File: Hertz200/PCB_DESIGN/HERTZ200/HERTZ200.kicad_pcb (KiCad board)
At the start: 2 copper layers, 7.1 x 7.3 mm, 99 parts, among them IC1 BD33HC5MEFJ-ME2, J1 SMA_CONNECTOR, J2 SIM_Card, J3 SMA_CONNECTOR, J4 DCJ250-10-A-K1-K, J5 USB_B_Micro, J6 GPIO_PINS, J7 SWD_PINS, Q1 Si2312DS, Q2 BC847, Q3 Si2312DS, Q4 CSD25302Q2, SW1 SW_Push, SW2 SW_Push, U1 STM32L431CCUx, U2 SIM7020E, U3 TXB0104PW, U4 SIM68M, U5 BQ24195LRGER, U6 HTS221

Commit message: layout02
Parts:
- C10, C14, C15, C2, C21, C22, C23, C24, C25, C26, C3, C4, C5, C6, C7, C8, C9, D4, D6, R25: moved to B.Cu
- SW2: footprint TS04-66-75-BK-160-SMT:SW_TS04-66-75-BK-160-SMT -> TL3305AF160QG:SW_TL3305AF160QG
- moved C3 139.2 mm to (53.4, 62.0), turned to 90 degrees
- moved FB1 135.7 mm to (52.8, 62.0), turned to -90 degrees
- moved SW1 132.1 mm to (43.5, 62.7), turned to 90 degrees
- moved C6 128.9 mm to (57.1, 55.4)
- moved C1 127.3 mm to (54.1, 59.8), turned to 180 degrees
- moved C7 124.0 mm to (64.7, 62.9), turned to 90 degrees
- moved C2 118.2 mm to (54.9, 62.0), turned to 90 degrees
- moved C24 116.9 mm to (57.7, 71.6), turned to -90 degrees
- moved J6 116.8 mm to (49.4, 69.6)
- moved J7 115.0 mm to (71.3, 46.1), turned to -90 degrees
- moved U1 114.8 mm to (59.8, 60.3)
- moved C5 113.7 mm to (62.4, 65.2), turned to 180 degrees
- moved J2 113.7 mm to (83.1, 77.1), turned to 180 degrees
- moved C4 113.6 mm to (64.7, 57.6), turned to -90 degrees
- moved R25 112.7 mm to (59.3, 65.2)
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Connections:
- C11 pad +: (no net) -> +3V3
- C11 pad -: (no net) -> GND
- C12 pad +: (no net) -> +3V3
- C12 pad -: (no net) -> GND
- J2 pad C1: (no net) -> /SIM7020E/SC_VCC
- J2 pad C2: (no net) -> /SIM7020E/RST_SC
- J2 pad C3: (no net) -> /SIM7020E/CLK_SC
- J2 pad C5: (no net) -> GND
- J2 pad C7: (no net) -> /SIM7020E/I/O_SC
- J2 pad G1: (no net) -> GND
- J2 pad G2: (no net) -> GND
- J2 pad G3: (no net) -> GND
- J2 pad G4: (no net) -> GND
- J2 pad G5: (no net) -> GND
- J2 pad G6: (no net) -> GND
- J7 pad 1: /STM32L431_MCU/SWCLK -> /STM32L431_MCU/SWDIO
- J7 pad 2: /STM32L431_MCU/SWDIO -> /STM32L431_MCU/SWCLK
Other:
- board size 7.1 x 7.3 mm -> 10.2 x 39.9 mm

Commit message: DRC
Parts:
- removed D10: BAT54C, Package_TO_SOT_SMD:SOT-23
- removed FB1: FerriteBead_Small, Inductor_SMD:L_0603_1608Metric
- removed SW1: SW_Push, TS04-66-75-BK-160-SMT:SW_TS04-66-75-BK-160-SMT
- removed SW2: SW_Push, TL3305AF160QG:SW_TL3305AF160QG
- added C41: 1uF, Capacitor_SMD:C_0805_2012Metric, B.Cu at (40.4, 61.7)
- added C42: 0.01uF, Capacitor_SMD:C_0603_1608Metric, B.Cu at (43.7, 62.8)
- added C43: 10uF, Capacitor_SMD:C_0603_1608Metric, B.Cu at (43.7, 66.5)
- added D9: ESD9L5.0ST5G, ESD9L5:DIOM1006X40N, F.Cu at (96.3, 72.2)
- added PS1: TAR5SB33_TE85L,F_, TAR5S33:SOT95P275X140-5N, B.Cu at (40.8, 64.6)
- added R2: 130R, Resistor_SMD:R_0805_2012Metric, B.Cu at (46.2, 66.0)
- added R24: 33K, Resistor_SMD:R_0603_1608Metric, F.Cu at (96.4, 78.4)
- added S1: TL3305AF160QG, TL3305AF160QG:SW_TL3305AF160QG, F.Cu at (43.7, 70.1)
- added S2: TL3305AF160QG, TL3305AF160QG:SW_TL3305AF160QG, F.Cu at (79.7, 36.0)
- C10, C2, C3, C5, C6, C7, C8, C9, D6, R25: moved to F.Cu
- C32, Q1, Q3, Q4, R13, R14, R15, R16, R19, R21, R26, R27: moved to B.Cu
- D3: value ESD -> LXES15AAA1-153; footprint Diode_SMD:D_0603_1608Metric -> Diode_SMD:D_0402_1005Metric
- D7: value SP0502BAHT -> ESD9L5.0ST5G; footprint Package_TO_SOT_SMD:SOT-23 -> ESD9L5:DIOM1006X40N
- J4: footprint DCJ250-10-A_XX-X_REVA:GCT_DCJ250-10-A_XX-X_REVA -> Connector_BarrelJack:BarrelJack_Horizontal
- J5: value USB_B_Micro -> 105164-0001; footprint Connector_USB:USB_Micro-B_Molex-105017-0001 -> 105164-0001:MOLEX_105164-0001
- moved R1 153.6 mm to (51.7, 61.8), turned to -90 degrees
- moved J4 123.6 mm to (40.0, 44.2), turned to 0 degrees
- moved U6 117.7 mm to (71.0, 66.8), turned to 180 degrees
- moved C39 112.9 mm to (37.1, 55.9), turned to 90 degrees
- moved Q4 110.3 mm to (49.3, 45.6), turned to 90 degrees
- moved R13 106.8 mm to (43.1, 45.8), turned to -90 degrees
- moved R16 106.6 mm to (47.0, 45.8), turned to 90 degrees
- moved R14 106.2 mm to (43.1, 49.3), turned to -90 degrees
- moved L2 106.2 mm to (54.9, 43.1)
- moved C36 105.4 mm to (54.9, 41.5), turned to 180 degrees
- moved C35 105.2 mm to (59.7, 41.1)
- moved C37 104.8 mm to (57.1, 40.6), turned to 90 degrees
- moved R17 104.4 mm to (54.7, 39.8), turned to 180 degrees
- moved R15 103.9 mm to (45.1, 45.8), turned to -90 degrees
- moved C31 103.2 mm to (54.1, 45.6), turned to 90 degrees
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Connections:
- C11 pad +: +3V3 -> (no net)
- C11 pad -: GND -> (no net)
- C12 pad +: +3V3 -> (no net)
- C12 pad -: GND -> (no net)
- J2 pad C1: /SIM7020E/SC_VCC -> (no net)
- J2 pad C2: /SIM7020E/RST_SC -> (no net)
- J2 pad C3: /SIM7020E/CLK_SC -> (no net)
- J2 pad C5: GND -> (no net)
- J2 pad C7: /SIM7020E/I/O_SC -> (no net)
- J2 pad G1: GND -> (no net)
- J2 pad G2: GND -> (no net)
- J2 pad G3: GND -> (no net)
- J2 pad G4: GND -> (no net)
- J2 pad G5: GND -> (no net)
- J2 pad G6: GND -> (no net)
- J4 pad 1: /BQ24195_SMPS/DC_JACK -> VIN
- J5 pad 1: /BQ24195_SMPS/USB_VBUS -> unconnected-(J5-Pad1)
- J5 pad 2: /BQ24195_SMPS/D- -> /SIM7020E/SIM7020E_D-
- J5 pad 3: /BQ24195_SMPS/D+ -> /SIM7020E/SIM7020E_D+
- J6 pad 2: VIN -> +3V3
- J6 pad 6: /STM32L431_MCU/GPIO04 -> /STM32L431_MCU/GPIO05
- J6 pad 7: /STM32L431_MCU/GPIO05 -> GND
- R1 pad 2: PWR_SIGNAL -> /STM32L431_MCU/VDDA
- U1 pad 18: /STM32L431_MCU/GPIO4 -> /STM32L431_MCU/GPIO05
- U1 pad 19: /STM32L431_MCU/GPIO5 -> unconnected-(U1-Pad19)
- U1 pad 25: unconnected-(U1-Pad25) -> /STM32L431_MCU/DRDY
- U1 pad 45: PWR_SIGNAL -> Signal_VOUT
- U2 pad 25: unconnected-(U2-Pad25) -> /SIM7020E/SIM7020E_D+
- U2 pad 26: unconnected-(U2-Pad26) -> /SIM7020E/SIM7020E_D-
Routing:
- net GND: track 0.00 -> 118.4 mm, vias 0 -> 128
- net /BQ24195_SMPS/OTG: track 0.00 -> 37.5 mm, vias 0 -> 3
- net SIM7020E_GPIO1: track 0.00 -> 31.0 mm, vias 0 -> 2
- net +3V3: track 0.00 -> 29.7 mm, vias 0 -> 31
- net /STM32L431_MCU/GPIO01: track 0.00 -> 29.1 mm
- net /STM32L431_MCU/GPIO02: track 0.00 -> 28.1 mm
- net /STM32L431_MCU/GPIO03: track 0.00 -> 27.1 mm
- net /SIM7020E/UART2_RDX: track 0.00 -> 26.4 mm, vias 0 -> 2
- net /SIM7020E/UART2_TXD: track 0.00 -> 26.2 mm, vias 0 -> 2
- net /STM32L431_MCU/MCU_LED: track 0.00 -> 26.1 mm, vias 0 -> 2
- net /STM32L431_MCU/GPIO05: track 0.00 -> 25.5 mm, vias 0 -> 1
- net /SIM7020E/VDD_EXT: track 0.00 -> 25.4 mm, vias 0 -> 3
- net /STM32L431_MCU/SWDIO: track 0.00 -> 24.3 mm
- net /STM32L431_MCU/SWO: track 0.00 -> 23.0 mm
- net /SIM7020E/SIM7020E_D+: track 0.00 -> 22.3 mm
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- added copper zone on F.Cu, net +3V3
- added copper zone on In2.Cu, net +3V3
- added copper zone on F.Cu, net /BQ24195_SMPS/BAT
- added copper zone on B.Cu, net /BQ24195_SMPS/PMID
- added copper zone on F.Cu, net /BQ24195_SMPS/PMID
- added copper zone on F.Cu, net /BQ24195_SMPS/SW
- added copper zone on F.Cu, net /BQ24195_SMPS/SYS
- added copper zone on B.Cu, net /BQ24195_SMPS/VBUS
- added copper zone on F.Cu, net /BQ24195_SMPS/VBUS
- added copper zone on F.Cu, net /SIM7020E/PWRKEY
- added copper zone on F.Cu, net /STM32L431_MCU/NRST
- added copper zone on F.Cu, net /STM32L431_MCU/VDDA
- added copper zone on B.Cu, net GND
- added copper zone on F.Cu, net GND
- added copper zone on In1.Cu, net GND
- added copper zone on B.Cu, net Net-(Q3-Pad1)
- added copper zone on B.Cu, net VIN
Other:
- board size 10.2 x 39.9 mm -> 72.1 x 56.1 mm
- copper layers 2 -> 4

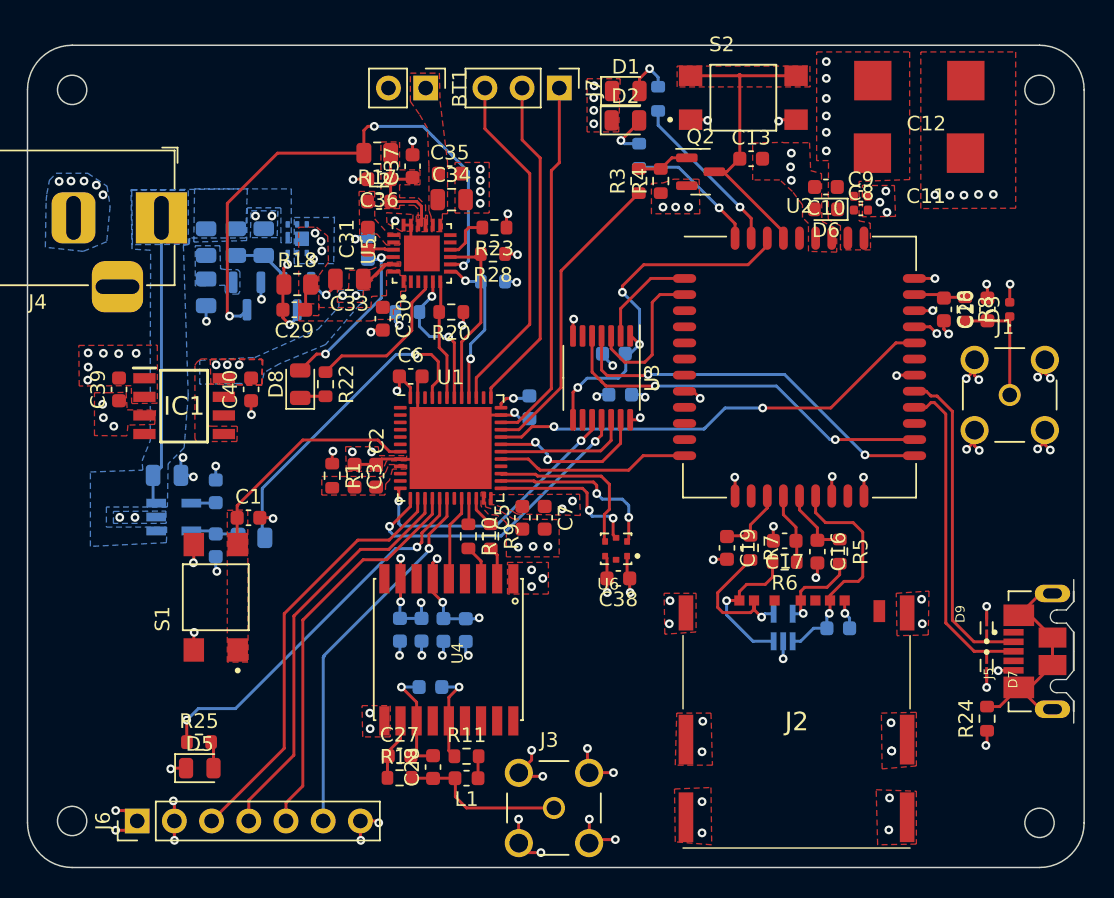
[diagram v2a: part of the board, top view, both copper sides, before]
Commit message: TEMPERATURE SENSOR ROUTING
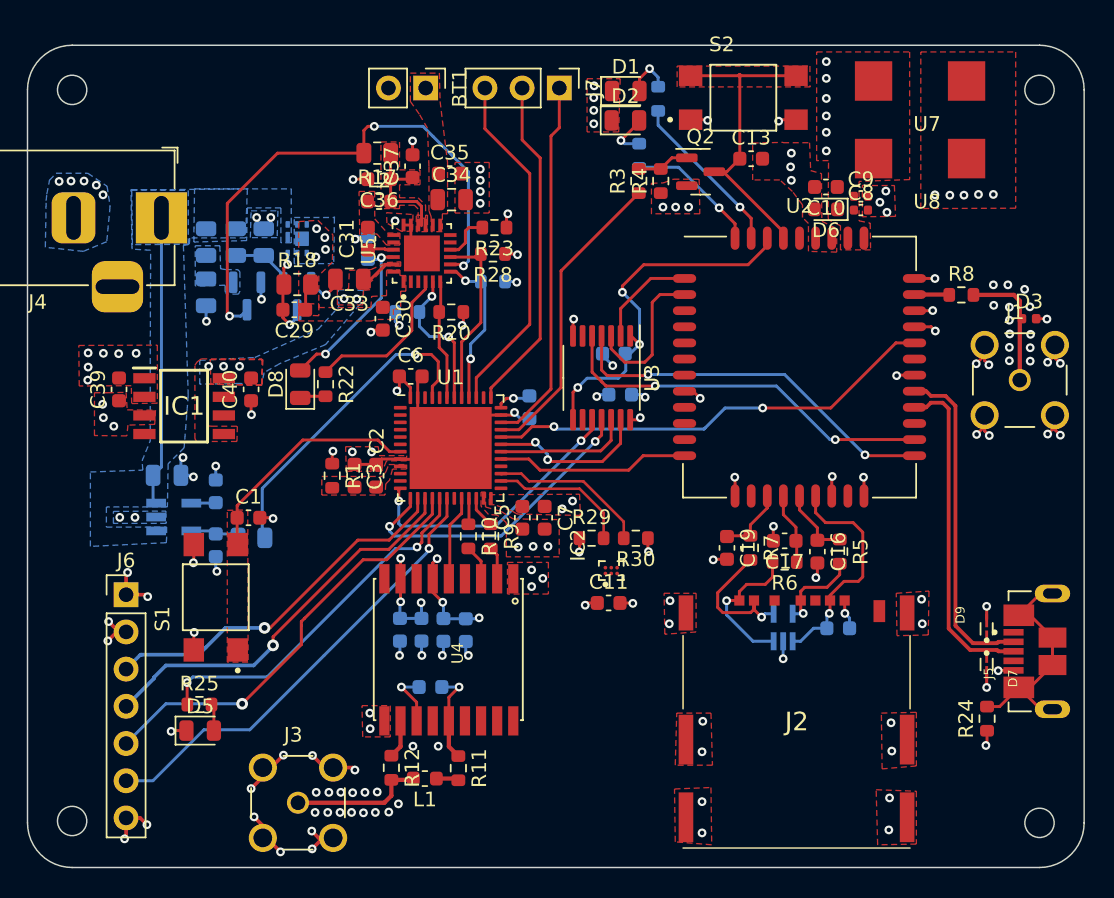
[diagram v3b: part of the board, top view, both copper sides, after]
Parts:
- removed C12: 100uF, T491X107K025AT:CAPMP7343X400N
- removed C18, C20, C27, C28: F, Capacitor_SMD:C_0603_1608Metric
- removed C38: 0.1uF, Capacitor_SMD:C_0603_1608Metric
- removed U6: HTS221, HTS221:XDCR_HTS221
- added IC2: TMP108AIYFFT, TMP108:TMP108AIYFFT, F.Cu at (70.7, 68.2)
- added R29: 5K, Resistor_SMD:R_0603_1608Metric, F.Cu at (69.4, 66.0)
- added R30: 5K, Resistor_SMD:R_0603_1608Metric, F.Cu at (72.4, 66.0)
- added U7: 100uF, T491X107K025AT:CAPMP7343X400N, F.Cu at (91.8, 34.8)
- added U8: 100uF, T491X107K025AT:CAPMP7343X400N, F.Cu at (91.8, 40.1)
- C11: value 100uF -> 0.1uF; footprint T491X107K025AT:CAPMP7343X400N -> Capacitor_SMD:C_0603_1608Metric
- J2: value SIM_Card -> 503960-0696
- moved C11 37.3 mm to (70.5, 70.5), turned to 0 degrees
- moved J3 17.5 mm to (49.3, 84.1)
- moved J6 15.5 mm to (37.6, 69.9), turned to 0 degrees
- moved L1 2.84 mm to (58.0, 82.4)
- moved D5 2.57 mm to (42.6, 79.2)
- moved R25 2.57 mm to (42.6, 77.4)
- moved D3 1.47 mm to (99.2, 51.1), turned to 0 degrees
- moved J1 1.23 mm to (98.6, 55.2)
- moved R8 1.02 mm to (94.6, 49.4), turned to 0 degrees
- moved R11 0.99 mm to (60.3, 81.7), turned to -90 degrees
- moved R12 0.88 mm to (55.7, 81.7), turned to -90 degrees
- moved D7 0.07 mm to (96.3, 74.7)
- moved D9 0.07 mm to (96.3, 72.2)
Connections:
- J2 pad C1: (no net) -> /SIM7020E/SC_VCC
- J2 pad C2: (no net) -> /SIM7020E/RST_SC
- J2 pad C3: (no net) -> /SIM7020E/CLK_SC
- J2 pad C5: (no net) -> GND
- J2 pad C6: (no net) -> unconnected-(J2-PadC6)
- J2 pad C7: (no net) -> /SIM7020E/I/O_SC
- J2 pad DL1: (no net) -> unconnected-(J2-PadDL1)
- J2 pad DS1: (no net) -> unconnected-(J2-PadDS1)
- J2 pad G1: (no net) -> GND
- J2 pad G2: (no net) -> GND
- J2 pad G3: (no net) -> GND
- J2 pad G4: (no net) -> GND
- J2 pad G5: (no net) -> GND
- J2 pad G6: (no net) -> GND
- U1 pad 26: /STM32L431_MCU/HTS221_SCL -> /STM32L431_MCU/TMP108_SCL
- U1 pad 27: /STM32L431_MCU/HTS221_SDA -> /STM32L431_MCU/TMP108_SDA
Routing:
- net /STM32L431_MCU/HTS221_SCL: track 12.3 -> 0.00 mm, vias 2 -> 0
- net /STM32L431_MCU/HTS221_SDA: track 11.8 -> 0.00 mm
- net /STM32L431_MCU/TMP108_SDA: track 0.00 -> 10.9 mm
- net /STM32L431_MCU/DRDY: track 10.7 -> 0.00 mm, vias 2 -> 0
- net /STM32L431_MCU/TMP108_SCL: track 0.00 -> 9.65 mm
- net GND: track 118.4 -> 109.9 mm, vias 128 -> 154
- net /STM32L431_MCU/GPIO05: track 25.5 -> 31.3 mm
- net /STM32L431_MCU/GPIO01: track 29.1 -> 25.3 mm, vias 0 -> 1
- net /STM32L431_MCU/GPIO03: track 27.1 -> 29.4 mm, vias 0 -> 1
- net Net-(J3-Pad1): track 11.3 -> 9.19 mm
- net Net-(R12-Pad1): track 4.26 -> 2.64 mm
- net /SIM7020E/ANT: track 3.57 -> 2.38 mm
- net /STM32L431_MCU/MCU_LED: track 26.1 -> 25.0 mm
- net /STM32L431_MCU/GPIO02: track 28.1 -> 27.3 mm, vias 0 -> 1
- net Net-(D3-Pad1): track 8.12 -> 8.74 mm
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
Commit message: ROUTE DONE
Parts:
- removed BT1: Battery_Cell, Connector_PinHeader_2.54mm:PinHeader_1x02_P2.54mm_Vertical
- removed C35: 0.1uF, Capacitor_SMD:C_0603_1608Metric
- removed C36, C37, C43: 10uF, Capacitor_SMD:C_0603_1608Metric
- removed C39, C40: 1uF, Capacitor_SMD:C_0603_1608Metric
- removed C41: 1uF, Capacitor_SMD:C_0805_2012Metric
- removed C42: 0.01uF, Capacitor_SMD:C_0603_1608Metric
- removed D8: LED_Small, LED_SMD:LED_0805_2012Metric
- removed J4: DCJ250-10-A-K1-K, Connector_BarrelJack:BarrelJack_Horizontal
- removed L2: 2.2uH, Inductor_SMD:L_0603_1608Metric
- removed Q1, Q3: Si2312DS, Package_TO_SOT_SMD:SOT-23
- removed Q4: CSD25302Q2, Package_SON:Texas_DQK
- removed R17, R18: 10K, Resistor_SMD:R_0805_2012Metric
- removed R19, R20, R21, R28: 10K, Resistor_SMD:R_0603_1608Metric
- removed R22: 2.2K, Resistor_SMD:R_0603_1608Metric
- removed R23: 100R, Resistor_SMD:R_0603_1608Metric
- added BT2: Battery_Cell, Connector_PinHeader_2.54mm:PinHeader_1x02_P2.54mm_Vertical, F.Cu at (48.1, 31.1)
- added C12: 22uF, Capacitor_SMD:C_1206_3216Metric, F.Cu at (39.2, 41.1)
- added C18: 1uF, Capacitor_SMD:C_0603_1608Metric, F.Cu at (41.1, 41.8)
- added C20: 1uF, Capacitor_SMD:C_0603_1608Metric, F.Cu at (43.1, 45.0)
- added C27: 0.1uF, Capacitor_SMD:C_0603_1608Metric, F.Cu at (44.3, 53.0)
- added C28: 0.1uF, Capacitor_SMD:C_0603_1608Metric, F.Cu at (41.5, 47.2)
- added C38: 22uF, Capacitor_SMD:C_1206_3216Metric, F.Cu at (47.0, 35.9)
- added C44: 22uF, Capacitor_SMD:C_1206_3216Metric, F.Cu at (49.4, 35.9)
- added C45: 22uF, Capacitor_SMD:C_1206_3216Metric, B.Cu at (54.1, 49.0)
- added C46: 22uF, Capacitor_SMD:C_1206_3216Metric, B.Cu at (56.4, 48.9)
- added C47: 1uF, Capacitor_SMD:C_0603_1608Metric, B.Cu at (58.3, 48.1)
- added C48: 1uF, Capacitor_SMD:C_0603_1608Metric, B.Cu at (59.8, 48.1)
- added D10: RED_LED, LED_SMD:LED_0603_1608Metric, F.Cu at (34.4, 62.1)
- added D11: BLUE_LED, LED_SMD:LED_0603_1608Metric, F.Cu at (40.5, 62.2)
- added D12: BLUE_LED, LED_SMD:LED_0603_1608Metric, F.Cu at (37.5, 62.1)
- added IC3: BQ29701DSET, BQ29701DSET:BQ29701DSET, F.Cu at (41.3, 30.9)
- added J8: USB4125-GF-A-0190_REVA2, USB4125-GF-A-0190_REVA2:GCT_USB4125-GF-A-0190_REVA2, F.Cu at (33.6, 43.6)
- added L3: 1.5uH, 744311150:WE-HCI_7030_7040_705023, F.Cu at (55.8, 41.2)
- added R33: 5.1K, Resistor_SMD:R_0603_1608Metric, F.Cu at (41.6, 50.3)
- added R34: 5.1K, Resistor_SMD:R_0603_1608Metric, F.Cu at (46.6, 53.0)
- added R35: 23.7K, Resistor_SMD:R_0603_1608Metric, F.Cu at (41.6, 51.8)
- added R36: 15K, Resistor_SMD:R_0603_1608Metric, F.Cu at (41.6, 53.3)
- added R37: 10K, Resistor_SMD:R_0603_1608Metric, F.Cu at (48.6, 40.8)
- added R38: 47.5K, Resistor_SMD:R_0603_1608Metric, F.Cu at (50.0, 53.0)
- added R39: 10K, Resistor_SMD:R_0603_1608Metric, F.Cu at (47.0, 40.8)
- added R40: 13.3K, Resistor_SMD:R_0603_1608Metric, F.Cu at (41.5, 48.7)
- added R41: 10K, Resistor_SMD:R_0603_1608Metric, F.Cu at (45.5, 40.8)
- added R42: 10K, Resistor_SMD:R_0603_1608Metric, F.Cu at (50.1, 40.8)
- added R43: 2K, Resistor_SMD:R_0603_1608Metric, B.Cu at (39.0, 62.2)
- added R44: 2K, Resistor_SMD:R_0603_1608Metric, B.Cu at (33.0, 62.1)
- added R45: 2K, Resistor_SMD:R_0603_1608Metric, B.Cu at (35.9, 62.1)
- added R46: 20m, Resistor_SMD:R_2512_6332Metric, F.Cu at (55.7, 35.2)
- added R47: 1K, Resistor_SMD:R_0603_1608Metric, F.Cu at (43.1, 41.8)
- added R48: 37.4K, Resistor_SMD:R_0603_1608Metric, F.Cu at (51.5, 53.1)
- added R49: 31.6K, Resistor_SMD:R_0603_1608Metric, B.Cu at (52.1, 48.2)
- added R50: 10K, Resistor_SMD:R_0603_1608Metric, F.Cu at (48.6, 53.0)
- added R51: 10K, Resistor_SMD:R_0603_1608Metric, B.Cu at (51.4, 50.5)
- added U6: MP2636GR-P, MP2636GR-P:IC_MP2636GR-P, F.Cu at (48.3, 47.0)
- added U9: CSD16406Q3, CSD16406Q3:TRANS_CSD16406Q3, F.Cu at (43.3, 36.1)
- C29: value 1nF -> 1uF; footprint Capacitor_SMD:C_0603_1608Metric -> Capacitor_SMD:C_0805_2012Metric; moved to B.Cu
- C30, IC1: moved to B.Cu
- C31: value 47nF -> 0.01uF; moved to B.Cu
- C32: value 4.7uF -> 10uF
- C33: value 10uF -> 1uF; footprint Capacitor_SMD:C_0805_2012Metric -> Capacitor_SMD:C_0603_1608Metric; moved to B.Cu
- C34: value 10uF -> 0.1uF; footprint Capacitor_SMD:C_0805_2012Metric -> Resistor_SMD:R_0805_2012Metric
- IC2: value TMP108AIYFFT -> TMP451HQDQWTQ1; footprint TMP108:TMP108AIYFFT -> Tmp451:SON50P250X200X80-8N
- Q2: value BC847 -> BC847-T
- R13: value 121K -> 2.2K; footprint Resistor_SMD:R_0805_2012Metric -> Resistor_SMD:R_0603_1608Metric; moved to F.Cu
- R14: value 49.9K -> 5.1M; footprint Resistor_SMD:R_0805_2012Metric -> Resistor_SMD:R_0603_1608Metric; moved to F.Cu
- R15: value 262K -> 5.1M; footprint Resistor_SMD:R_0805_2012Metric -> Resistor_SMD:R_0603_1608Metric; moved to F.Cu
- R16: value 100K -> 330R; moved to F.Cu
- R29, R30: value 5K -> 10K
- U5: value BQ24195LRGER -> CSD16406Q3; footprint BQ24195RGER:QFN50P400X400X100-25N -> CSD16406Q3:TRANS_CSD16406Q3
- moved IC1 25.8 mm to (65.8, 48.1), turned to 180 degrees
- moved U5 21.1 mm to (39.4, 36.1), turned to -90 degrees
- moved C34 20.7 mm to (44.1, 29.4)
- moved C32 19.7 mm to (37.4, 56.7)
- moved C31 16.3 mm to (38.9, 51.5)
- moved C29 16.2 mm to (32.9, 51.2), turned to -90 degrees
- moved R14 16.0 mm to (43.0, 33.2), turned to 180 degrees
- moved R13 15.6 mm to (38.8, 30.8), turned to 0 degrees
- moved C30 15.5 mm to (70.3, 48.0), turned to 90 degrees
- moved R16 14.7 mm to (44.1, 31.4), turned to 0 degrees
- moved R15 14.0 mm to (39.0, 33.3), turned to 0 degrees
- moved PS1 12.3 mm to (36.0, 53.3)
- moved R2 11.7 mm to (39.9, 56.1)
- moved C33 8.44 mm to (61.3, 48.0), turned to 90 degrees
- moved C11 3.21 mm to (70.3, 73.7)
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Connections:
- C29 pad 1: /BQ24195_SMPS/VBUS -> GND
- C29 pad 2: Net-(C29-Pad2) -> /MP2636/VIN
- C30 pad 1: /BQ24195_SMPS/VBUS -> GND
- C30 pad 2: GND -> +3V3
- C31 pad 2: /BQ24195_SMPS/SW -> GND
- C32 pad 1: /BQ24195_SMPS/REGN -> GND
- C32 pad 2: GND -> Net-(C32-Pad2)
- C33 pad 1: /BQ24195_SMPS/PMID -> GND
- C33 pad 2: GND -> +5V
- C34 pad 1: /BQ24195_SMPS/BAT -> Net-(C34-Pad1)
- IC1 pad 5: /BQ24195_SMPS/PMID -> +5V
- IC1 pad 8: /BQ24195_SMPS/PMID -> +5V
- PS1 pad 1: VIN -> /MP2636/VIN
- PS1 pad 3: VIN -> /MP2636/VIN
- PS1 pad 4: Net-(C42-Pad1) -> Net-(C31-Pad1)
- PS1 pad 5: Net-(C43-Pad2) -> Net-(C32-Pad2)
- R13 pad 1: VIN -> GND
- R13 pad 2: Net-(Q3-Pad1) -> Net-(IC3-Pad6)
- R14 pad 1: Net-(Q3-Pad1) -> GND
- R14 pad 2: GND -> /MP2636/DOUT
- R15 pad 1: VIN -> GND
- R15 pad 2: Net-(Q1-Pad1) -> /MP2636/COUT
- R16 pad 1: Net-(Q1-Pad1) -> Net-(C34-Pad1)
- R16 pad 2: GND -> /MP2636/BATT
- R2 pad 2: Net-(C43-Pad2) -> Net-(C32-Pad2)
- R29 pad 2: /STM32L431_MCU/TMP108_SCL -> /STM32L431_MCU/TMP451_SCL
- R30 pad 2: /STM32L431_MCU/TMP108_SDA -> /STM32L431_MCU/TMP451_SDA
- U1 pad 26: /STM32L431_MCU/TMP108_SCL -> /STM32L431_MCU/TMP451_SCL
- U1 pad 27: /STM32L431_MCU/TMP108_SDA -> /STM32L431_MCU/TMP451_SDA
- U5 pad 1: /BQ24195_SMPS/VBUS -> GND
- U5 pad 2: /BQ24195_SMPS/D+ -> GND
- U5 pad 3: /BQ24195_SMPS/D- -> GND
- U5 pad 4: /BQ24195_SMPS/STAT -> /MP2636/COUT
- U5 pad 5: PMIC_SCL -> Net-(U5-Pad5)
- U5 pad 6: PMIC_SDA -> Net-(U5-Pad5)
- U5 pad 7: PMIC_INT -> Net-(U5-Pad5)
- U5 pad 8: /BQ24195_SMPS/OTG -> Net-(U5-Pad5)
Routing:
- net Net-(D10-Pad1): track 0.00 -> 41.0 mm, vias 0 -> 2
- net /BQ24195_SMPS/OTG: track 37.5 -> 0.00 mm, vias 3 -> 0
- net /MP2636/VCC: track 0.00 -> 35.8 mm, vias 0 -> 2
- net /MP2636/BATT: track 0.00 -> 33.8 mm, vias 0 -> 2
- net Net-(D11-Pad1): track 0.00 -> 32.6 mm, vias 0 -> 2
- net Net-(L3-Pad2): track 0.00 -> 23.0 mm
- net VIN: track 19.8 -> 0.00 mm
- net Net-(D12-Pad1): track 0.00 -> 19.5 mm
- net /MP2636/VIN: track 0.00 -> 16.2 mm, vias 0 -> 1
- net /STM32L431_MCU/TMP451_SDA: track 0.00 -> 15.1 mm
- net Net-(R49-Pad2): track 0.00 -> 14.3 mm, vias 0 -> 1
- net /STM32L431_MCU/TMP451_SCL: track 0.00 -> 13.5 mm
- net PMIC_CE: track 12.7 -> 0.00 mm
- net GND: track 109.9 -> 122.0 mm, vias 154 -> 170
- net /BQ24195_SMPS/REGN: track 12.2 -> 0.00 mm, vias 2 -> 0
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- added copper zone on B.Cu, net +3V3
- added copper zone on B.Cu, net +5V
- added copper zone on F.Cu, net +5V
- added copper zone on F.Cu, net /MP2636/BATT
- added copper zone on F.Cu, net /MP2636/FB
- added copper zone on F.Cu, net /MP2636/VCC
- added copper zone on F.Cu, net /MP2636/VIN
- added copper zone on F.Cu, net Net-(L3-Pad1)
- added copper zone on F.Cu, net Net-(L3-Pad2)
- added copper zone on F.Cu, net Net-(R33-Pad2)
- added copper zone on F.Cu, net Net-(R34-Pad2)
- added copper zone on F.Cu, net Net-(R40-Pad1)
- removed copper zone on F.Cu, net /BQ24195_SMPS/BAT
- removed copper zone on B.Cu, net /BQ24195_SMPS/PMID
- removed copper zone on F.Cu, net /BQ24195_SMPS/PMID
- removed copper zone on F.Cu, net /BQ24195_SMPS/SW
- removed copper zone on F.Cu, net /BQ24195_SMPS/SYS
- removed copper zone on B.Cu, net /BQ24195_SMPS/VBUS
- removed copper zone on F.Cu, net /BQ24195_SMPS/VBUS
- removed copper zone on B.Cu, net Net-(Q3-Pad1)
- removed copper zone on B.Cu, net VIN
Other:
- board size 72.1 x 56.1 mm -> 72.3 x 61.5 mm
